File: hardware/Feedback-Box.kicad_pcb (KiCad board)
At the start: 2 copper layers, 100 x 50 mm, 84 parts, among them J1 694106301002, J2 UJ2-BH-1-TH, J3 T821106A1S100CEU, J4 SSW-104-01-T-S, Q1 FDN340P, Q2 FDN340P, Q3 MMBT2222ALT1G, Q4 FDN340P, Q5 FDN340P, Q6 FDN340P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

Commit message: Started on Hardware Layout
Power & Loudspeaker sections done. Provisional layout of USB and most connectors also done.
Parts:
- removed the REF** at (196.0, 74.0)
- removed the REF** at (196.0, 116.0)
- removed the REF** at (104.0, 116.0)
- removed the REF** at (104.0, 74.0)
- added G***: LOGO, Feedback-Box:SI-Logo-W32.5mm_H13.5mm, F.Cu at (121.3, 161.9)
- added H1: MountingHole_2.2mm_M2, MountingHole:MountingHole_2.2mm_M2, F.Cu at (102.5, 72.5)
- added H2: MountingHole_2.2mm_M2, MountingHole:MountingHole_2.2mm_M2, F.Cu at (102.5, 117.5)
- added H3: MountingHole_2.2mm_M2, MountingHole:MountingHole_2.2mm_M2, F.Cu at (197.5, 72.5)
- added H4: MountingHole_2.2mm_M2, MountingHole:MountingHole_2.2mm_M2, F.Cu at (197.5, 117.5)
- added REF**: WEEE-Logo_4.2x6mm_SilkScreen, Symbol:WEEE-Logo_4.2x6mm_SilkScreen, F.Cu at (127.0, 174.5)
- added REF**: OSHW-Logo_5.7x6mm_SilkScreen, Symbol:OSHW-Logo_5.7x6mm_SilkScreen, F.Cu at (114.5, 174.5)
- added REF**: ESD-Logo_6.6x6mm_SilkScreen, Symbol:ESD-Logo_6.6x6mm_SilkScreen, F.Cu at (121.0, 174.5)
- C10: moved to B.Cu
- moved R1 172.0 mm to (209.8, 54.0), turned to 180 degrees
- moved R2 171.2 mm to (213.8, 54.0), turned to 180 degrees
- moved C12 141.2 mm to (245.1, 109.9)
- moved R10 141.2 mm to (256.9, 112.4)
- moved R22 141.2 mm to (257.4, 107.3)
- moved R27 141.2 mm to (268.4, 111.1)
- moved R29 141.2 mm to (256.9, 103.5)
- moved R30 141.2 mm to (240.4, 111.1)
- moved R6 141.2 mm to (240.4, 116.2)
- moved R8 141.2 mm to (263.3, 117.5)
- moved Q5 141.2 mm to (250.2, 107.3)
- moved Q6 141.2 mm to (262.9, 106.0)
- moved Q7 141.2 mm to (262.9, 112.4)
- moved R11 141.2 mm to (247.3, 103.5)
- moved R21 141.2 mm to (251.9, 112.4)
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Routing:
- net GND: track 0.00 -> 186.9 mm, vias 0 -> 2
- net GNDS: track 0.00 -> 59.4 mm
- net +5V: track 0.00 -> 51.5 mm, vias 0 -> 3
- net BAT: track 0.00 -> 49.1 mm
- net Net-(D2-Pad1): track 0.00 -> 29.1 mm
- net Net-(Q3-Pad2): track 0.00 -> 23.5 mm
- net USBD-: track 0.00 -> 21.4 mm
- net USBD+: track 0.00 -> 20.2 mm
- net USB~RST: track 0.00 -> 18.3 mm
- net Net-(Q2-Pad1): track 0.00 -> 18.1 mm, vias 0 -> 2
- net Net-(BT1-Pad1): track 0.00 -> 17.6 mm
- net Net-(DS1-Pad3): track 0.00 -> 15.7 mm
- net SPK: track 0.00 -> 13.3 mm
- net Net-(C5-Pad1): track 0.00 -> 12.8 mm
- net +3V3: track 0.00 -> 11.4 mm
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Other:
- outline, holes or cut-outs redrawn
- net class Power added: clearance 0.3, trace_width 0.4, via_dia 0.8, via_drill 0.4
- rule trace_min: 0.2 -> 0.127
- rule via_min_size: 0.4 -> 0.6
- board text added: "Part No SI-FBCM01-6A github.com/Alarm-Siren/Feedback-Box © Nicholas Parks Young, 2020. Some Rights Reserved."
- board text added: "Volume"

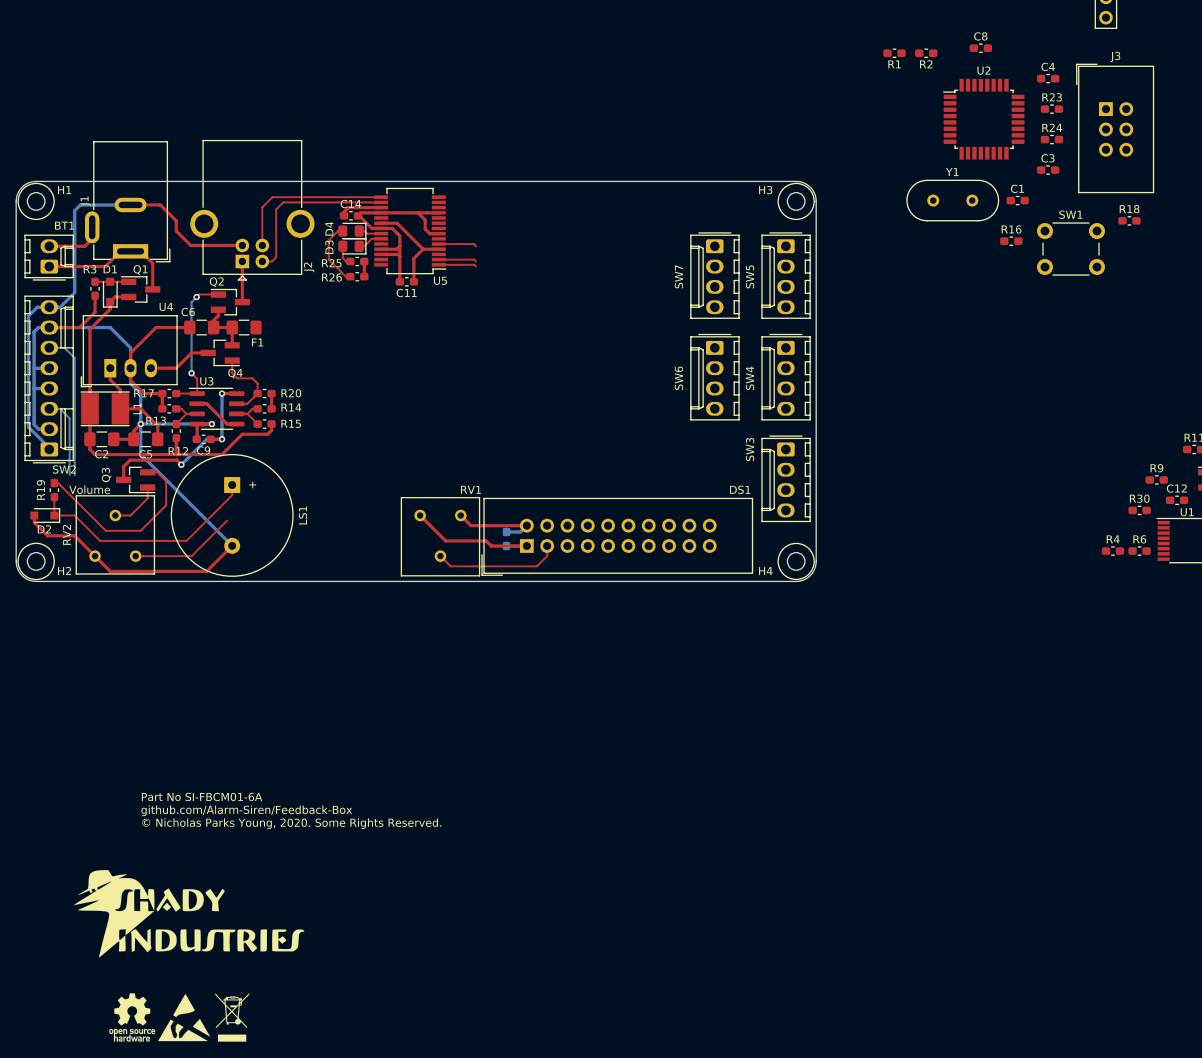
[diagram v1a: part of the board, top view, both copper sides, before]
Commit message: Labelled up the Power/Audio, routed a bit more power
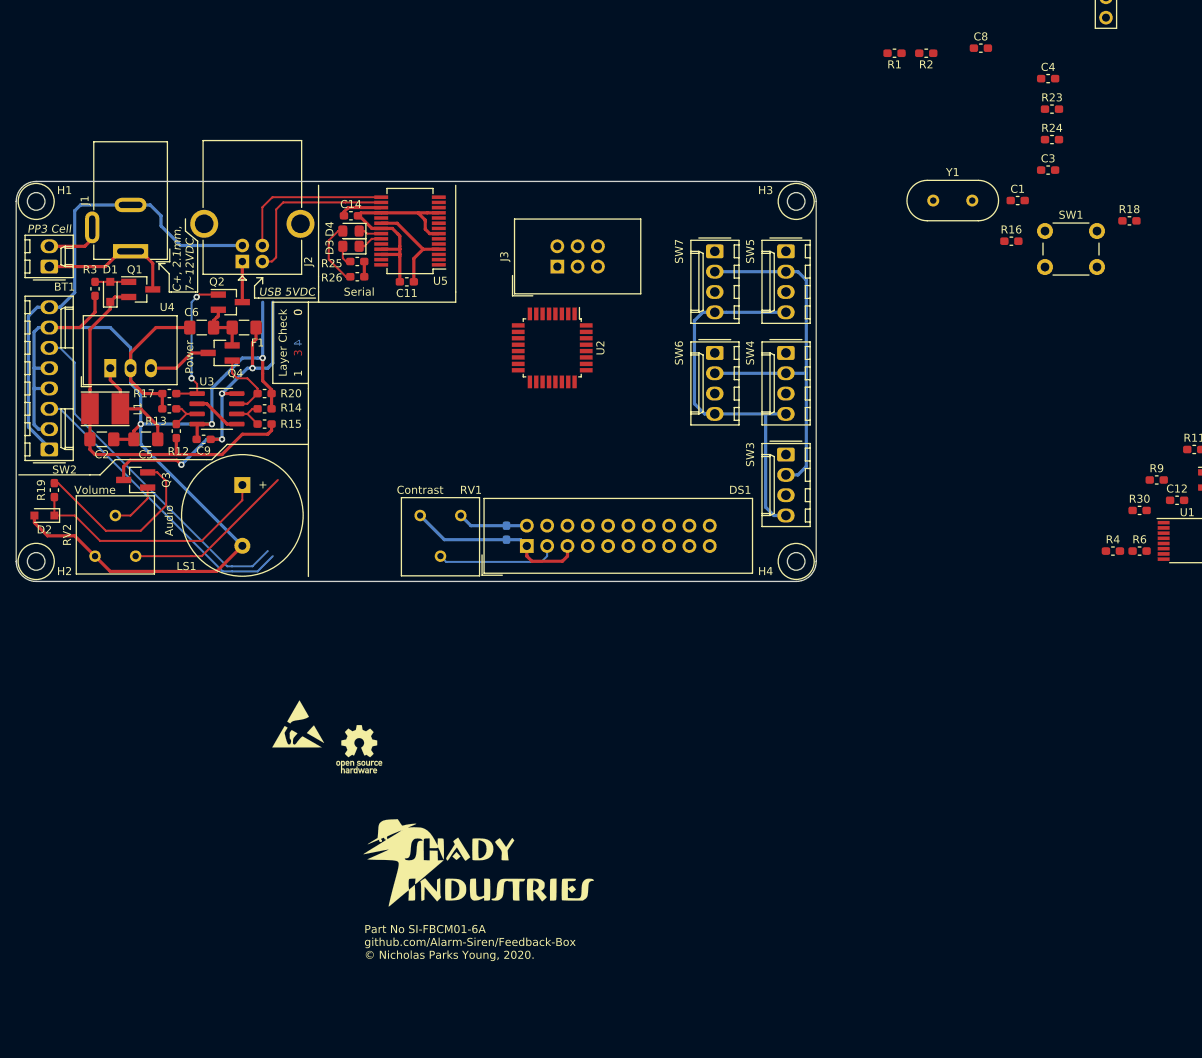
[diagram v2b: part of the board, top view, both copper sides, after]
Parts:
- removed the REF** at (127.0, 174.5)
- moved J3 71.3 mm to (167.6, 80.6), turned to 90 degrees
- moved U2 61.1 mm to (167.0, 90.8), turned to 270 degrees
- moved REF** 43.9 mm to (142.9, 141.0)
- moved REF** 39.4 mm to (135.3, 137.8)
- moved G*** 36.7 mm to (157.5, 155.6)
- moved LS1 1.27 mm to (128.3, 108.0)
- moved C10 0.79 mm to (161.3, 113.9)
- moved SW3 0.64 mm to (196.2, 104.1)
- moved SW4 0.63 mm to (196.2, 91.4)
- moved SW5 0.63 mm to (196.2, 78.7)
- moved SW6 0.63 mm to (187.3, 91.4)
- moved SW7 0.63 mm to (187.3, 78.7)
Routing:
- net GND: track 186.9 -> 267.9 mm, vias 2 -> 3
- net +5V: track 51.5 -> 118.3 mm, vias 3 -> 4
- net PROG~EN: track 10.1 -> 37.1 mm
- net USB~RST: track 18.3 -> 43.2 mm
- net SPK: track 13.3 -> 21.7 mm
- net TXD: track 4.77 -> 0.00 mm
- net ~DTR: track 4.75 -> 0.00 mm
- net RXD: track 4.75 -> 0.00 mm
- net Net-(D2-Pad1): track 29.1 -> 30.7 mm
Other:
- board text added: "+"
- board text added: "-"
- board text added: "0"
- board text added: "1"
- board text added: "10"
- board text added: "2"
- board text added: "20"
- board text added: "3"
- board text added: "4"
- board text added: "5"
- board text added: "5VDC"
- board text added: "6"
- board text added: "7V~~12VDC"
- board text added: "9VDC"
- board text added: "Audio"
- board text added: "C+, 2.1mm, 7~~12VDC"
- board text added: "Contrast"
- board text added: "GND"
- board text added: "Layer Check"
- board text added: "PP3 Cell"
- board text added: "Part No SI-FBCM01-6A github.com/Alarm-Siren/Feedback-Box © Nicholas Parks Young, 2020."
- board text added: "Power"
- board text added: "Serial"
- board text added: "USB 5VDC"
- board text added: "Vin"
- board text added: "Vout"
- board text removed: "Part No SI-FBCM01-6A github.com/Alarm-Siren/Feedback-Box © Nicholas Parks Young, 2020. Some Rights Reserved."

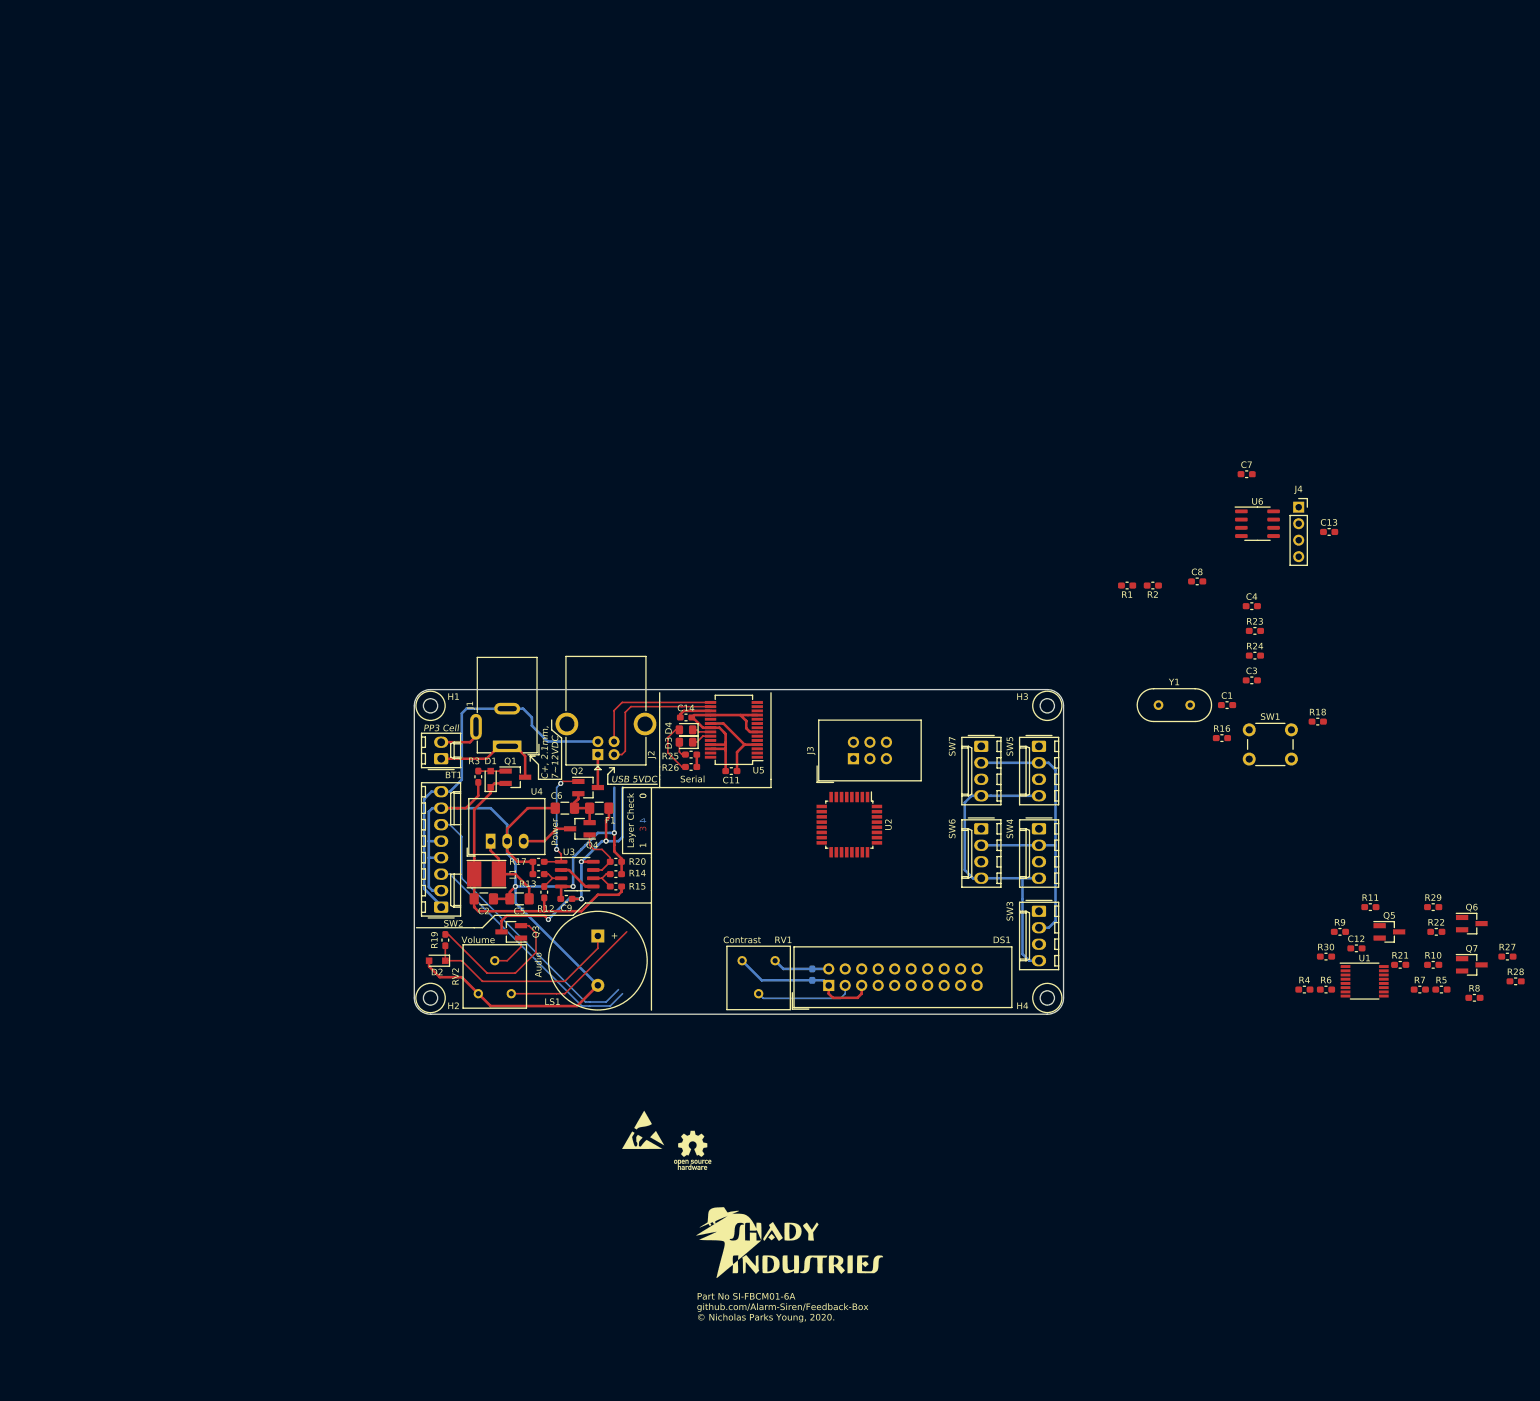
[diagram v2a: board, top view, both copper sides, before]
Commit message: Mostly finished layout, just needs a little final routing
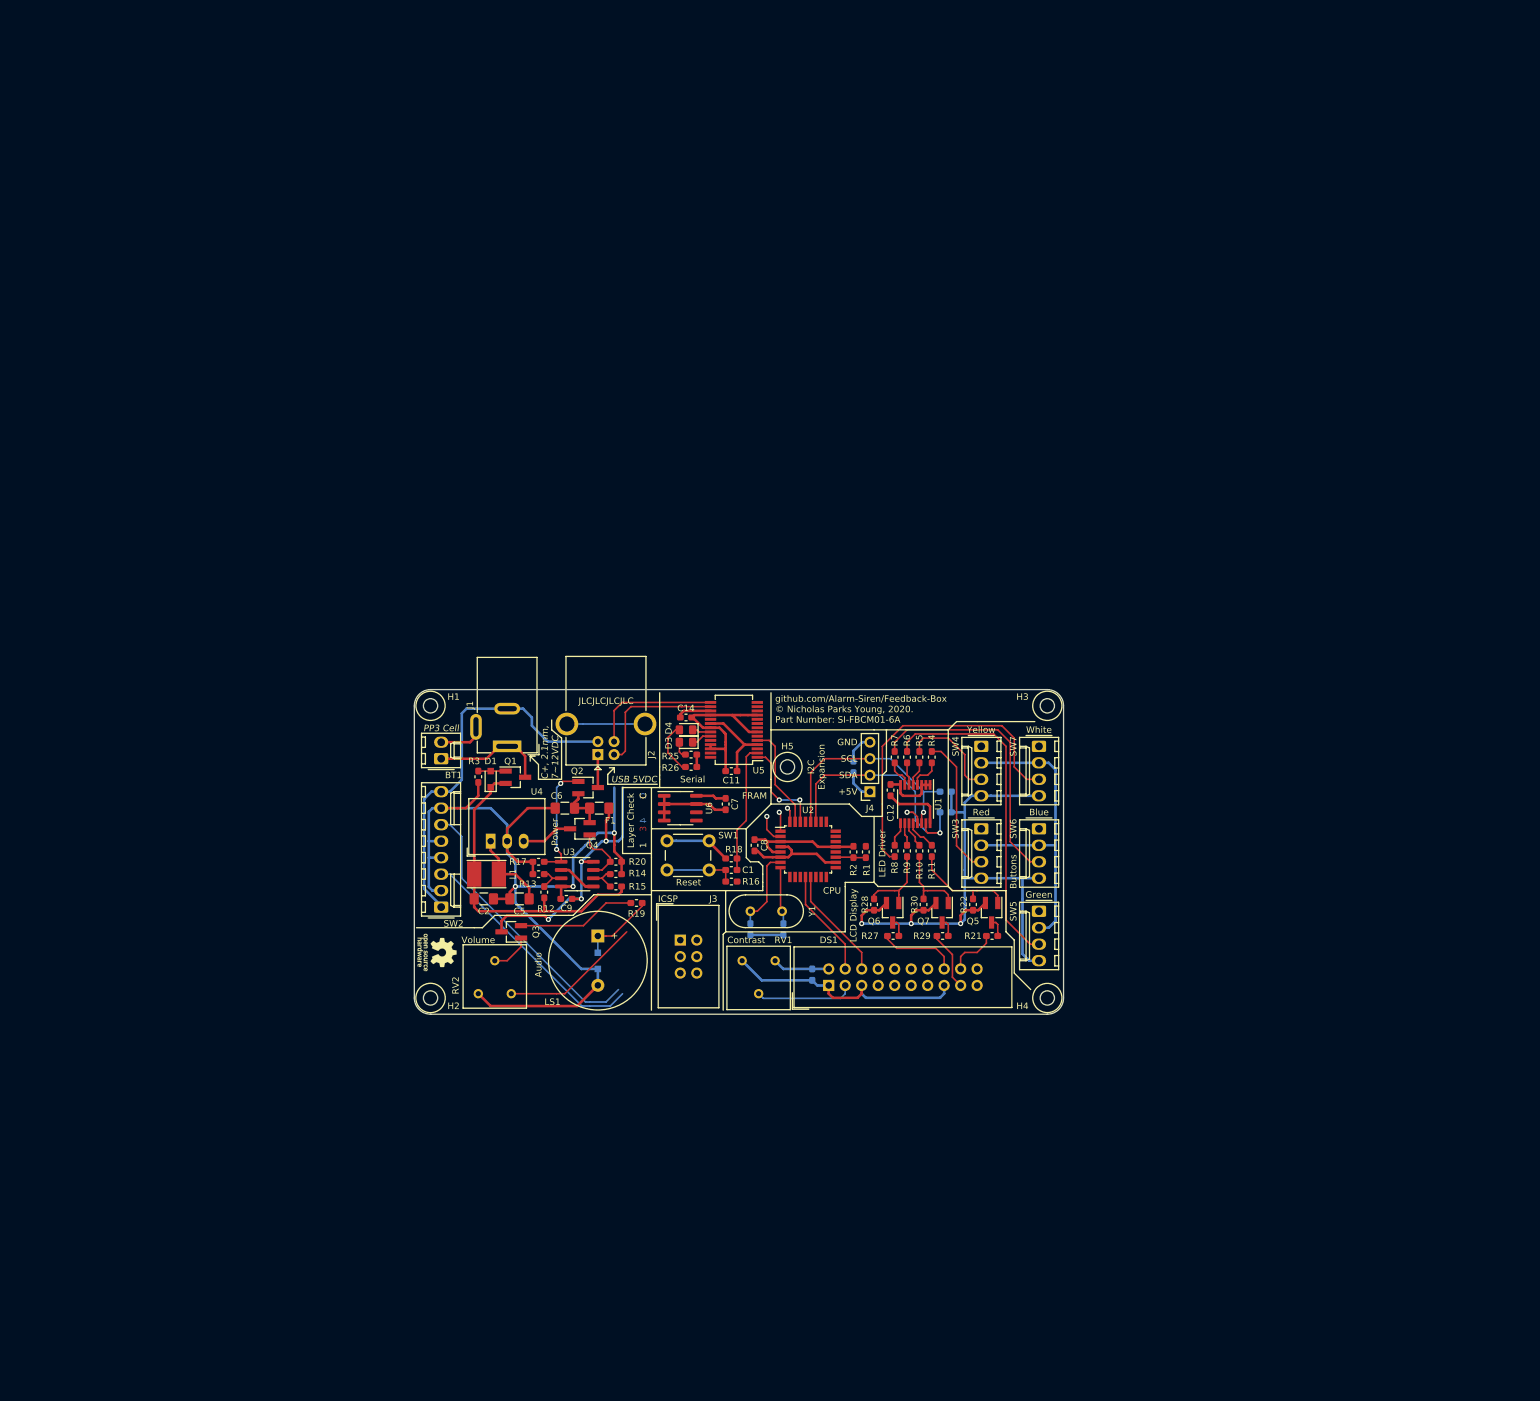
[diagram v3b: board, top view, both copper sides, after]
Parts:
- removed G***: LOGO, Feedback-Box:SI-Logo-W32.5mm_H13.5mm
- removed REF**: OSHW-Logo_5.7x6mm_SilkScreen, Symbol:OSHW-Logo_5.7x6mm_SilkScreen
- removed REF**: ESD-Logo_6.6x6mm_SilkScreen, Symbol:ESD-Logo_6.6x6mm_SilkScreen
- added G1: LOGO, Feedback-Box:SI-Logo-W32.5mm_H13.5mm, B.Cu at (160.7, 137.8)
- added G2: OSHW-Logo_5.7x6mm_SilkScreen, Symbol:OSHW-Logo_5.7x6mm_SilkScreen, F.Cu at (103.5, 110.5)
- added H5: MountingHole_2.2mm_M2, MountingHole:MountingHole_2.2mm_M2, F.Cu at (157.5, 81.9)
- C13, C3, C4, D2, R23, R24: moved to B.Cu
- moved R28 99.5 mm to (170.8, 103.1), turned to 270 degrees
- moved U6 99.1 mm to (141.0, 88.3)
- moved C7 95.0 mm to (148.0, 87.6), turned to 270 degrees
- moved R27 94.7 mm to (173.8, 108.0), turned to 180 degrees
- moved R18 92.8 mm to (148.8, 96.0)
- moved R8 92.1 mm to (174.0, 94.9), turned to 90 degrees
- moved Q6 89.2 mm to (173.7, 104.4), turned to 270 degrees
- moved R7 88.5 mm to (174.0, 80.4), turned to 270 degrees
- moved R5 88.0 mm to (177.8, 80.4), turned to 270 degrees
- moved C4 87.7 mm to (156.8, 106.9), turned to 90 degrees
- moved C3 86.2 mm to (151.8, 106.9), turned to 90 degrees
- moved SW1 85.9 mm to (145.4, 97.8), turned to 180 degrees
- moved Q7 82.0 mm to (181.3, 104.4), turned to 270 degrees
- moved C13 81.7 mm to (167.6, 81.9), turned to 90 degrees
- moved R10 81.1 mm to (177.8, 94.9), turned to 90 degrees
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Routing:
- net +5V: track 118.3 -> 199.3 mm, vias 4 -> 7
- net GND: track 267.9 -> 335.4 mm
- net LED3: track 0.00 -> 51.4 mm
- net LED5: track 0.00 -> 49.7 mm
- net LED4: track 0.00 -> 41.8 mm
- net SDA: track 0.00 -> 38.5 mm, vias 0 -> 1
- net SCL: track 0.00 -> 35.5 mm, vias 0 -> 1
- net LED1: track 0.00 -> 21.8 mm
- net ~DTR: track 0.00 -> 20.0 mm
- net Net-(D2-Pad1): track 30.7 -> 11.8 mm
- net LCD_E: track 0.00 -> 17.4 mm
- net LCD_RS: track 0.00 -> 16.7 mm
- net SCR_B-: track 0.00 -> 16.3 mm
- net TXD: track 0.00 -> 16.0 mm
- net LED2: track 0.00 -> 15.7 mm
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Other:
- net class Power: clearance 0.3 -> 0.2
- board text added: "+5V"
- board text added: "Blue"
- board text added: "Buttons"
- board text added: "C"
- board text added: "CPU"
- board text added: "FRAM"
- board text added: "Green"
- board text added: "I2C Expansion"
- board text added: "ICSP"
- board text added: "JLCJLCJLCJLC"
- board text added: "LCD Display"
- board text added: "LED Driver"
- board text added: "Red"
- board text added: "Reset"
- board text added: "SCL"
- board text added: "SDA"
- board text added: "White"
- board text added: "Yellow"
- board text added: "github.com/Alarm-Siren/Feedback-Box © Nicholas Parks Young, 2020. Part Number: SI-FBCM01-6A"
- board text added: "www.shadyindustries.com"
- board text removed: "0"
- board text removed: "Part No SI-FBCM01-6A github.com/Alarm-Siren/Feedback-Box © Nicholas Parks Young, 2020."
